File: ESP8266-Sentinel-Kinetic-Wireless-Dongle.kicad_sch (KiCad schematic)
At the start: 61 parts, among them J1 Conn_01x04, J2 Screw_Terminal_01x04, J3 Conn_01x06_Pin, J4 RJ9, J5 Screw_Terminal_01x03, J6 Screw_Terminal_01x04, Q1 SS8050, Q2 AO3401A, Q3 AO3400A, SW2 SW_Push, SW4 SW_Push, U1 AMS1117-3.3, U2 ESP-12E, U3 MAX3232, U4 ESP32-WROOM-32, U5 L78L10_SOT89, U6 74AHCT125

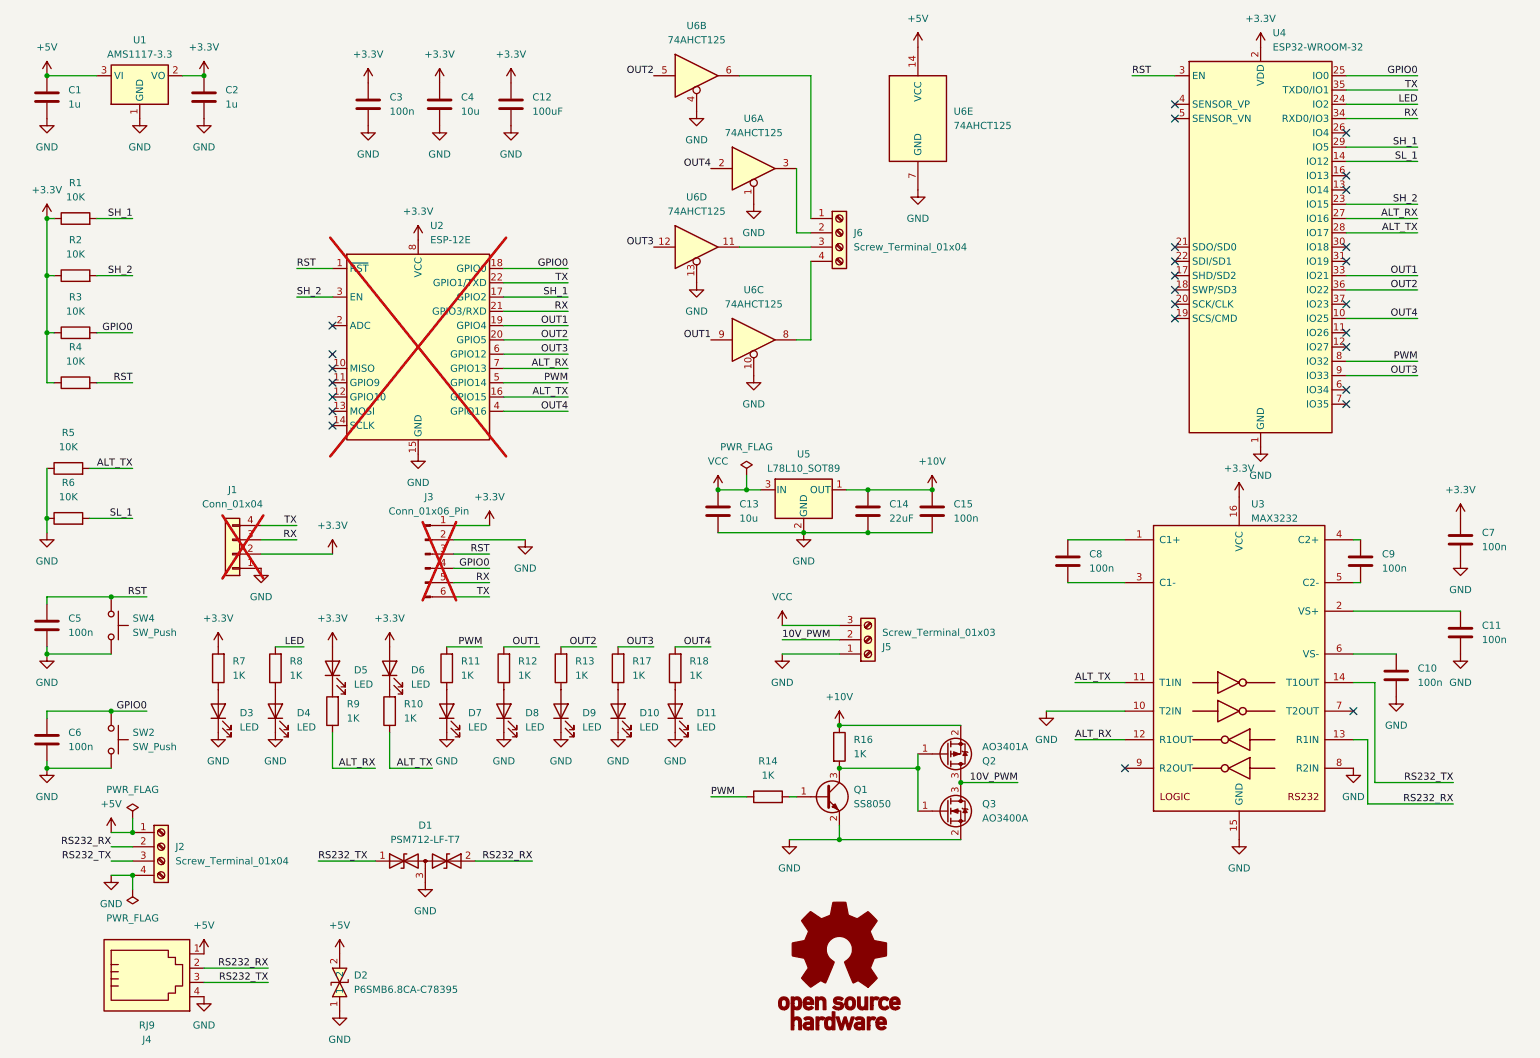
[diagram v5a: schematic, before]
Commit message: Applied fixes to issues from V1 Inverted LED's on UART to indicate only when data is sent Added Second UART to allow passthrough Removed support for ESP8266
Still need to add:
pin breakout for user mods
Buck regulator from 24V. We need more current on the 5V rail than available, if we expect anything else to be connected up (and not cause a brown out)
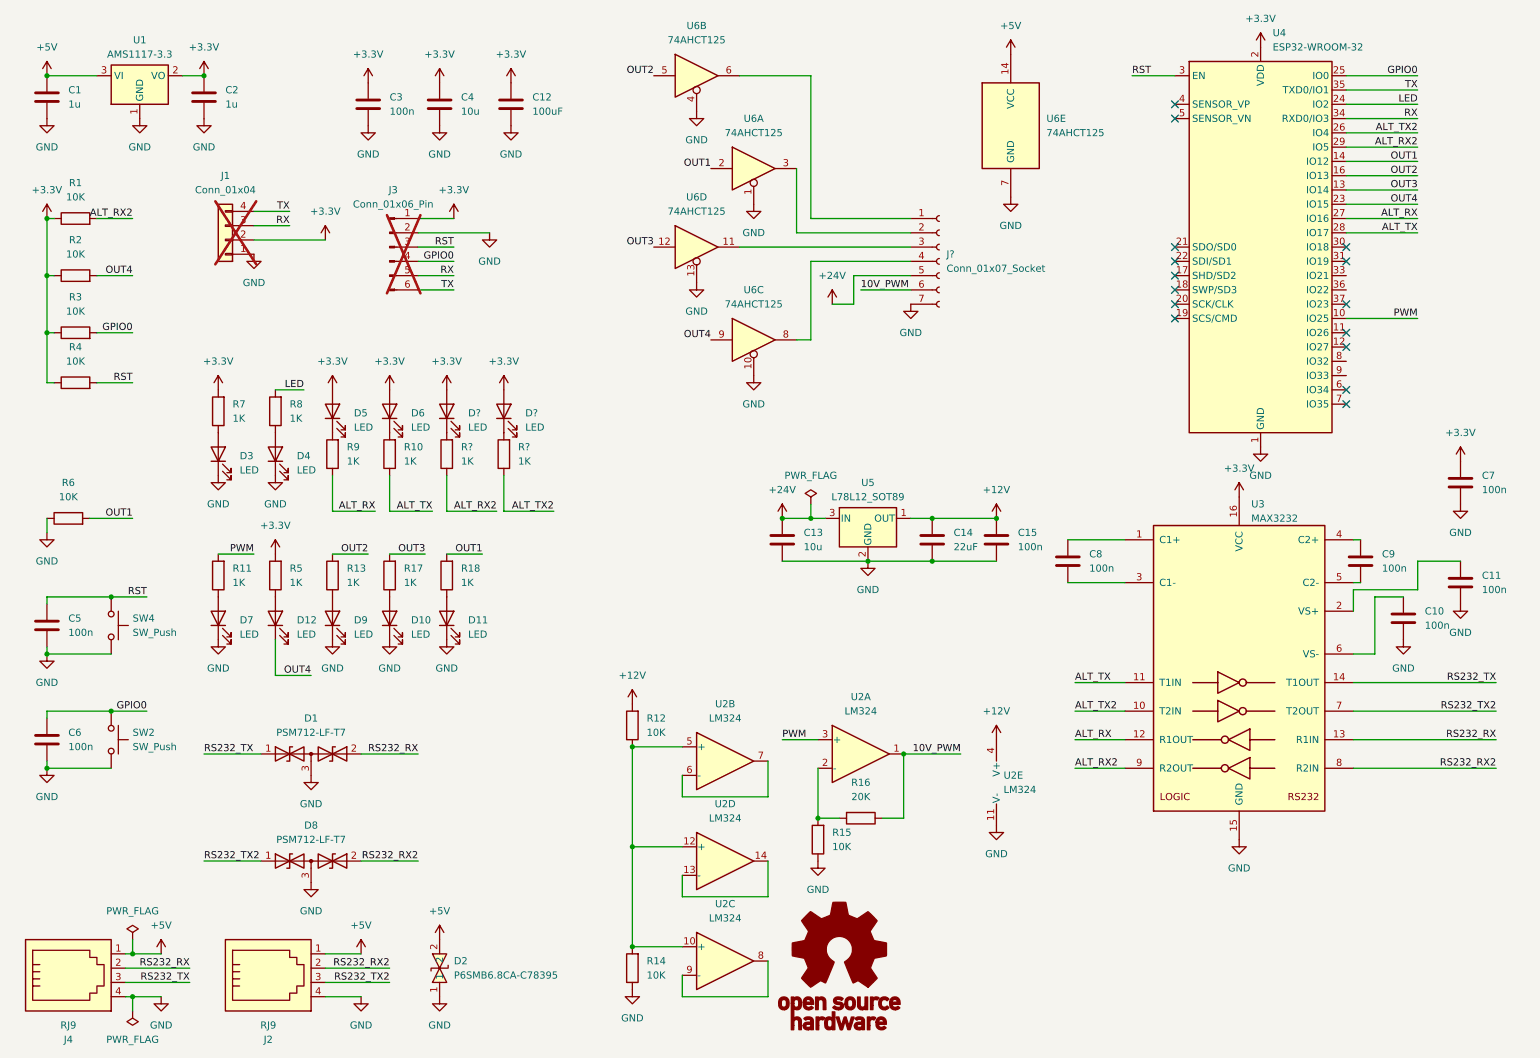
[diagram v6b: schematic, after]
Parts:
- removed D8: LED, LED_SMD:LED_0603_1608Metric, symbol Device:LED
- removed J2, J6: Screw_Terminal_01x04, TerminalBlock_4Ucon:TerminalBlock_4Ucon_1x04_P3.50mm_Horizontal, symbol Connector:Screw_Terminal_01x04
- removed J5: Screw_Terminal_01x03, TerminalBlock_4Ucon:TerminalBlock_4Ucon_1x03_P3.50mm_Horizontal, symbol Connector:Screw_Terminal_01x03
- removed Q1: SS8050, Package_TO_SOT_SMD:SOT-23, symbol Transistor_BJT:SS8050
- removed Q2: AO3401A, Package_TO_SOT_SMD:SOT-23, symbol Transistor_FET:AO3401A
- removed Q3: AO3400A, Package_TO_SOT_SMD:SOT-23, symbol Transistor_FET:AO3400A
- removed U2: ESP-12E, lib:ESP-12E, symbol lib:ESP-12E
- removed U5: L78L10_SOT89, Package_TO_SOT_SMD:SOT-89-3, symbol Regulator_Linear:L78L10_SOT89
- added D12, D? (x2): LED, LED_SMD:LED_0603_1608Metric, symbol Device:LED
- added D8: PSM712-LF-T7, Package_TO_SOT_SMD:SOT-23, symbol Device:D_TVS_Dual_AAC
- added J2: RJ9, lib:RJ9-TH-623K-4P4CGRAYBOUNDLESS, symbol Connector:RJ9
- added J?: Conn_01x07_Socket, Connector_JST:JST_XH_B7B-XH-AM_1x07_P2.50mm_Vertical, symbol Connector:Conn_01x07_Socket
- added R15: 10K, Resistor_SMD:R_0402_1005Metric, symbol Device:R
- added R? (x2): 1K, Resistor_SMD:R_0402_1005Metric, symbol Device:R
- added U2: LM324, Package_SO:SOIC-14_3.9x8.7mm_P1.27mm, symbol Amplifier_Operational:LM324
- added U5: L78L12_SOT89, Package_TO_SOT_SMD:SOT-89-3, symbol Regulator_Linear:L78L12_SOT89
- R12, R14: value 1K -> 10K; LCSC C11702 -> C25744
- R16: value 1K -> 20K; LCSC C11702 -> C25765
- R5: value 10K -> 1K; LCSC C25744 -> C11702
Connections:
- net SH_1 is gone; now on net ALT_RX2: R1.2, U4.29 (IO5)
- net SH_2 is gone; now on net OUT4: R2.2, U4.23 (IO15)
- net SL_1 is gone; now on net OUT1: R6.2, U4.14 (IO12)
- net +3.3V: now also R5.2, D?.2 (A), D?.2 (A)
- net +5V: now also J2.1
- net 10V_PWM: now also R16.1, J?.6 (Pin_6), U2.1
- net ALT_TX: no longer R5.2
- net GND: now also R14.1, D8.3 (common), J2.4, J?.7 (Pin_7), R15.1, U2.11 (V-), U5.2 (GND); no longer R5.1, U3.10 (T2IN), U3.8 (R2IN)
- net OUT1: now also R18.2, U6.2; no longer R12.2, U4.33 (IO21), U6.9
- net OUT2: now also U4.16 (IO13); no longer U4.36 (IO22)
- net OUT3: now also U4.13 (IO14); no longer U4.9 (IO33)
- net OUT4: now also U6.9, D12.1 (K); no longer R18.2, U4.10 (IO25), U6.2
- net PWM: now also U4.10 (IO25), U2.3 (+); no longer R14.1, U4.8 (IO32)
- net at R14.2: now also R12.1, U2.10 (+), U2.12 (+), U2.5 (+)
- net at R16.2: now also R15.2, U2.2 (-)
- net at U6.8: now also J?.4 (Pin_4)
- net at U6.11: now also J?.3 (Pin_3)
- net at U6.3: now also J?.2 (Pin_2)
- net at U6.6: now also J?.1 (Pin_1)
- net ALT_TX2: now reaches U4.26 (IO4)
- net ALT_TX2: now also U3.10 (T2IN), R?.1
- net RS232_TX2: now reaches U3.7 (T2OUT)
- net RS232_TX2: now also D8.1 (A1), J2.3
- net ALT_RX2: now reaches U3.9 (R2OUT)
- net ALT_RX2: now also R?.1
- net +10V renamed +12V
- net +12V: now also R12.2, U2.4 (V+), U5.1 (OUT); no longer R16.1
- net VCC renamed +24V
- net +24V: now also J?.5 (Pin_5), U5.3 (IN)
- new net: U2.8, U2.9 (-)
- new net: D12.2 (A), R5.1
- new net: U2.6 (-), U2.7
- new net: D?.1 (K), R?.2 (x2)
- new net: U2.13 (-), U2.14
- new net RS232_RX2: D8.2 (A2), J2.2, U3.8 (R2IN)
- no-connect marks 27 -> 15
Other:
- moved on the sheet: C10, C11, C13, C14, C15, C7, D1, D10, D11, D2, D3, D4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

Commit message: Layout completed Revesed RJ9 pinout to match Display Module Added reverse polarity protection diode to 24V rail Using OpAMP for 3.3 to 5V conversion Using OpAmp for 3.3 to 10V conversion JST XH for Mode 02 Control instead of screw terminals Added 5v 3A Buck regulator PMOD connector for spare GPIO Added I2C header
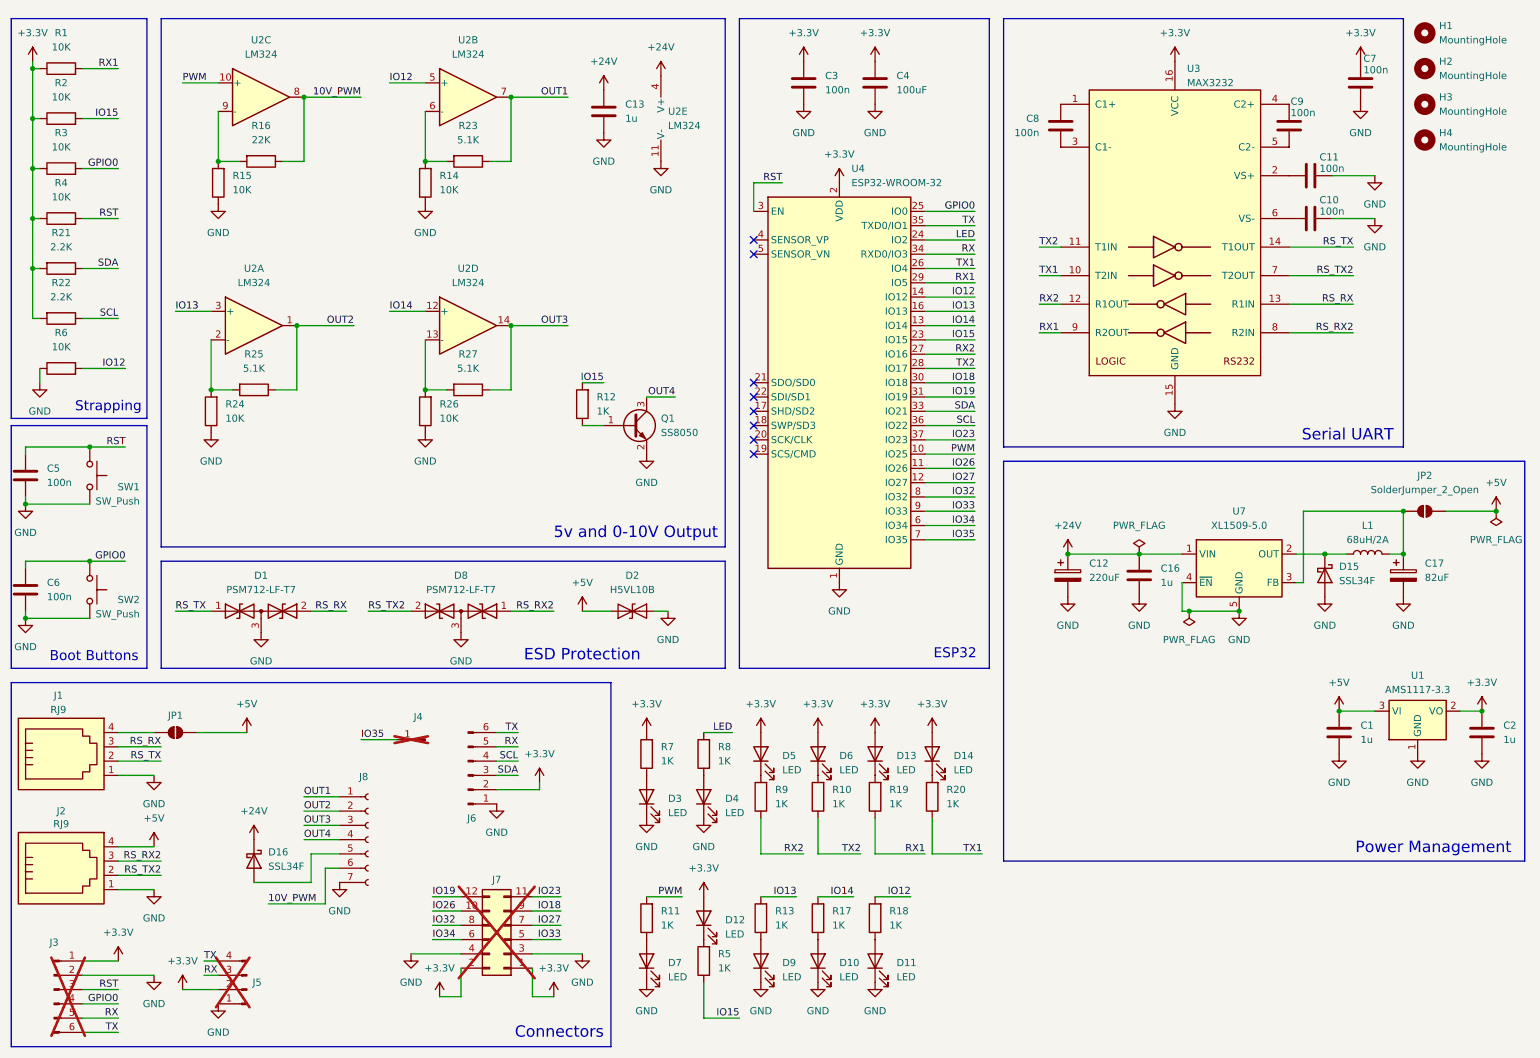
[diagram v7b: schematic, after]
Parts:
- removed C14: 22uF, Capacitor_SMD:C_0805_2012Metric, symbol Device:C
- removed C15: 100n, Capacitor_SMD:C_0402_1005Metric, symbol Device:C
- removed C4: 10u, Capacitor_SMD:C_0402_1005Metric, symbol Device:C
- removed D2: P6SMB6.8CA-C78395, lib:SMB_L4.6-W3.6-LS5.3-BI, symbol lib:P6SMB6.8CA-C78395
- removed G1: OSHW_Logo, SparkFun-Aesthetic:Creative_Commons_License, symbol SparkFun-Aesthetic:OSHW_Logo
- removed J1: Conn_01x04, SparkFun-Connector:1x04_Locking, symbol SparkFun-Connector:Conn_01x04_Locking
- removed U5: L78L12_SOT89, Package_TO_SOT_SMD:SOT-89-3, symbol Regulator_Linear:L78L12_SOT89
- removed U6: 74AHCT125, Package_DIP:DIP-14_W7.62mm, symbol 74xx:74AHCT125
- added C12: 220uF, Capacitor_THT:CP_Radial_D10.0mm_P5.00mm, symbol Device:C_Polarized
- added C16: 1u, Capacitor_SMD:C_1206_3216Metric, symbol Device:C
- added C17: 82uF, Capacitor_THT:CP_Radial_D10.0mm_P2.50mm_P5.00mm, symbol Device:C_Polarized
- added D15, D16: SSL34F, Diode_SMD:D_SMA, symbol Device:D_Schottky
- added D2: H5VL10B, Diode_SMD:D_SOD-882, symbol Diode:ESD9B3.3ST5G
- added H1, H2, H3, H4: MountingHole, MountingHole:MountingHole_3.2mm_M3, symbol Mechanical:MountingHole
- added J4: Conn_01x01_Pin, Connector_PinHeader_2.54mm:PinHeader_1x01_P2.54mm_Vertical, symbol Connector:Conn_01x01_Pin
- added J5: Conn_01x04_Pin, Connector_PinHeader_2.54mm:PinHeader_1x04_P2.54mm_Vertical, symbol Connector:Conn_01x04_Pin
- added J6: Conn_01x06_Pin, Connector_JST:JST_XH_B6B-XH-A_1x06_P2.50mm_Vertical, symbol Connector:Conn_01x06_Pin
- added J7: Conn_02x06_Odd_Even, Connector_PinHeader_2.54mm:PinHeader_2x06_P2.54mm_Vertical, symbol Connector_Generic:Conn_02x06_Odd_Even
- added JP1, JP2: SolderJumper_2_Open, Jumper:SolderJumper-2_P1.3mm_Open_RoundedPad1.0x1.5mm, symbol Jumper:SolderJumper_2_Open
- added L1: 68uH/2A, Inductor_SMD:L_APV_APH0850, symbol Device:L
- added Q1: SS8050, Package_TO_SOT_SMD:SOT-23, symbol Transistor_BJT:SS8050
- added R21, R22: 2.2K, Resistor_SMD:R_0402_1005Metric, symbol Device:R
- added R23, R25, R27: 5.1K, Resistor_SMD:R_0402_1005Metric, symbol Device:R
- added R24, R26: 10K, Resistor_SMD:R_0402_1005Metric, symbol Device:R
- added U7: XL1509-5.0, Package_SO:SOIC-8_3.9x4.9mm_P1.27mm, symbol Regulator_Switching:XL1509-5.0
- C13: value 10u -> 1u; LCSC C13585 -> C1848
- J8: renamed from J?; footprint Connector_JST:JST_XH_B7B-XH-AM_1x07_P2.50mm_Vertical -> Connector_JST:JST_XH_B7B-XH-A_1x07_P2.50mm_Vertical
- R12: value 10K -> 1K; LCSC C25744 -> C11702
- R16: value 20K -> 22K; LCSC C25765 -> C25768
- gave numbers to parts that had none: 4
- renumbered C12 to C4, J4 to J1, SW4 to SW1
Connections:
- net +24V: now also U2.4 (V+), C12.1, C16.1, D16.1 (K), U7.1 (VIN); no longer J8.5 (Pin_5)
- net +3.3V: now also D12.2 (A), J5.2 (Pin_2), J6.2 (Pin_2), J7.1 (Pin_1), J7.2 (Pin_2), R21.2, R22.2; no longer R5.2
- net +5V: now also J2.4, D2.1 (A1), JP1.2 (B), JP2.2 (B); no longer J1.1, J2.1
- net 10V_PWM: now also U2.8; no longer U2.1
- net GND: now also J1.1, J2.1, C12.2, C16.2, C17.2, D15.2 (A), D2.2 (A2), J5.1 (Pin_1), J6.1 (Pin_1), J7.3 (Pin_3), J7.4 (Pin_4), Q1.2 (E), R24.1, R26.1, U7.4 (~{EN}), U7.5 (GND), U7.6 (GND), U7.7 (GND), U7.8 (GND); no longer J1.4, J2.4
- net OUT1: now also J8.1 (Pin_1), U2.7, R23.1; no longer R18.2, R6.2, U4.14 (IO12)
- net OUT2: now also J8.2 (Pin_2), U2.1, R25.1; no longer R13.2, U4.16 (IO13)
- net OUT3: now also J8.3 (Pin_3), U2.14, R27.1; no longer R17.2, U4.13 (IO14)
- net OUT4: now also J8.4 (Pin_4), Q1.3 (C); no longer D12.1 (K), R2.2, U4.23 (IO15)
- net PWM: now also U2.10 (+); no longer U2.3 (+)
- net RX: now also J5.3 (Pin_3), J6.5 (Pin_5)
- net TX: now also J5.4 (Pin_4), J6.6 (Pin_6)
- net at U2.9 (-): now also R15.2, R16.2; no longer U2.8
- net IO15: now reaches R5.1
- net IO15: now also R12.2, R2.2, U4.23 (IO15); no longer D12.2 (A)
- net at U2.6 (-): now also R14.2, R23.2; no longer U2.7
- net at U2.13 (-): now also R26.2, R27.2; no longer U2.14
- net IO26: now reaches U4.11 (IO26)
- net IO26: now also J7.10 (Pin_10)
- net IO27: now reaches U4.12 (IO27)
- net IO27: now also J7.7 (Pin_7)
- net IO18: now reaches U4.30 (IO18)
- net IO18: now also J7.9 (Pin_9)
- net IO19: now reaches U4.31 (IO19)
- net IO19: now also J7.12 (Pin_12)
- net SDA: now reaches U4.33 (IO21)
- net SDA: now also J6.3 (Pin_3), R21.1
- net SCL: now reaches U4.36 (IO22)
- net SCL: now also J6.4 (Pin_4), R22.1
- net IO23: now reaches U4.37 (IO23)
- net IO23: now also J7.11 (Pin_11)
- net IO34: now reaches U4.6 (IO34)
- net IO34: now also J7.6 (Pin_6)
- net IO35: now reaches U4.7 (IO35)
- net IO35: now also J4.1 (Pin_1)
- net IO32: now reaches U4.8 (IO32)
- net IO32: now also J7.8 (Pin_8)
- net IO33: now reaches U4.9 (IO33)
- net IO33: now also J7.5 (Pin_5)
- removed net +12V: R12.2, U2.4 (V+)
- net ALT_RX renamed RX2
- net ALT_RX2 renamed RX1
- net ALT_TX renamed TX2
- net ALT_TX2 renamed TX1
- net RS232_RX renamed RS_RX
- net RS_RX: now also J1.3; no longer J1.2
- net RS232_RX2 renamed RS_TX2
- net RS_TX2: now also U3.7 (T2OUT); no longer U3.8 (R2IN)
- net RS232_TX renamed RS_TX
- net RS_TX: now also J1.2; no longer J1.3
- net RS232_TX2 renamed RS_RX2
- net RS_RX2: now also U3.8 (R2IN); no longer U3.7 (T2OUT)
- new net: D15.1 (K), L1.1, U7.2 (OUT)
- new net: C17.1, JP2.1 (A), L1.2, U7.3 (FB)
- new net: R24.2, R25.2, U2.2 (-)
- new net: D12.1 (K), R5.2
- new net: Q1.1 (B), R12.1
- new net: J1.4, JP1.1 (A)
- new net: D16.2 (A), J8.5 (Pin_5)
- new net IO12: R18.2, R6.2, U2.5 (+), U4.14 (IO12)
- new net IO13: R13.2, U2.3 (+), U4.16 (IO13)
- new net IO14: R17.2, U2.12 (+), U4.13 (IO14)
- no-connect marks 15 -> 8
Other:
- note added: "5v and 0-10V Output"
- note added: "Boot Buttons"
- note added: "Connectors"
- note added: "ESD Protection"
- note added: "ESP32"
- note added: "Power Management"
- note added: "Serial UART"
- note added: "Strapping"
- moved on the sheet: C1, C10, C11, C2, C3, C4, C5, C6, C7, C8, C9, D1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
